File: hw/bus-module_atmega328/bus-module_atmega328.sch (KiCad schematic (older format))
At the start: 32 parts, among them J1 CONN_10X2, J2 CONN_7X2, J3 CONN-ISP-6, J5 CONN_1, J6 CONN_1, J7 CONN_1, J8 CONN_1, U1 ATMEGA328-TQFP32, U2 7,3728MHz, U3 25LC256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

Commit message: R2, R3, R4 100 Ohms
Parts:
- F1: symbol bus-module_atmega328-rescue:FUSE -> bus-module_atmega328-rescue:FUSE-bus-module_atmega328-rescue
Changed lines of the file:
@@
 B
 $Comp
-L bus-module_atmega328-rescue:FUSE F1
+L bus-module_atmega328-rescue:FUSE-bus-module_atmega328-rescue F1
 U 1 1 56648405
 P 8950 1200

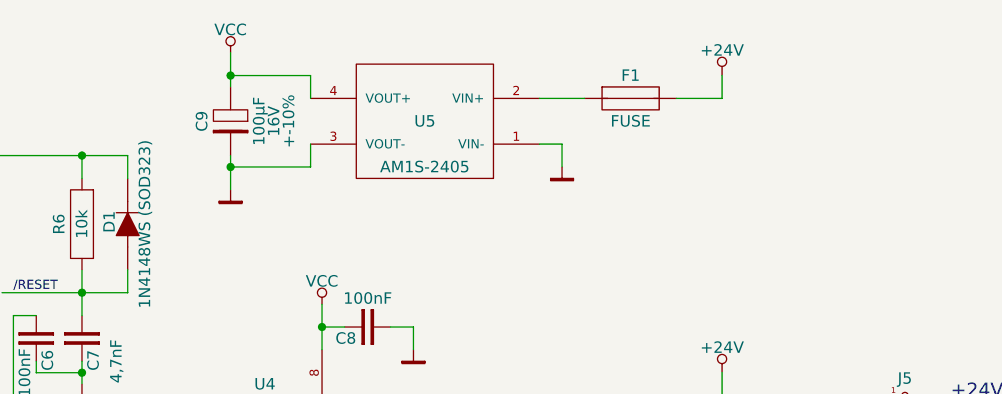
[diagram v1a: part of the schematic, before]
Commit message: Increase WAGO hole diameter, replace ELKO with keramic capacitor, Increase WAGO hole diameter, update footprints, update footprints, set Rev to C
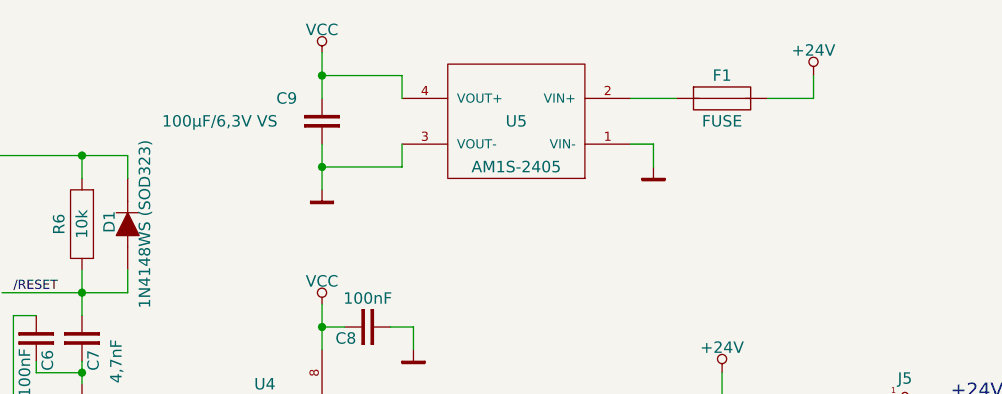
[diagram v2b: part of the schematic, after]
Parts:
- removed C9: 100µF, Capacitors:cp_smd_6.3, symbol standard:CP
- added C9: 100µF/6,3V VS, Capacitors_SMD:C_1206, symbol standard:C
- C1, C2, C3, C5, C6, C7, C8: footprint Housings_SOIC:SM0805 -> Capacitors_SMD:C_0805
- D1: footprint Diode:SOD323 -> Diode_SMD:D_SOD323
- D2: footprint Diode_SMD:SOT143 -> Diode_SMD:D_SOT143
- J5, J6, J7, J8: footprint Connector_Miscelleaneus:WAGO243 -> Connector_WAGO:WAGO243
- L1: footprint Housings_SOIC:SM0805 -> Inductor:L_0805
- R1, R2, R3, R4, R5, R6: footprint Housings_SOIC:SM0805 -> Resistor:R_0805
- U2: footprint Crystal:HC49-SMD -> Crystal:CRY_HC49_SMD
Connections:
- net GND: now also C9.2
- net VCC: now also C9.1
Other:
- moved on the sheet: F1, U5
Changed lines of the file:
@@
 Sheet 1 1
 Title "bus-module_atmega328"
-Date "2018-09-22"
-Rev "B"
+Date "2019-03-06"
+Rev "C"
 Comp "KoeWiBa"
 Comment1 ""
@@
 F 0 "J5" H 10150 2575 50  0000 C CNN
 F 1 "CONN_1" H 10150 2425 25  0000 C CNN
-F 2 "Connector_Miscelleaneus:WAGO243" H 10150 2500 60  0001 C CNN
+F 2 "Connector_WAGO:WAGO243" H 10150 2500 60  0001 C CNN
 F 3 "" H 10150 2500 60  0000 C CNN
 	1    10150 2500
@@
 F 0 "J6" H 10150 2775 50  0000 C CNN
 F 1 "CONN_1" H 10150 2625 25  0000 C CNN
-F 2 "Connector_Miscelleaneus:WAGO243" H 10150 2700 60  0001 C CNN
+F 2 "Connector_WAGO:WAGO243" H 10150 2700 60  0001 C CNN
 F 3 "" H 10150 2700 60  0000 C CNN
 	1    10150 2700
@@
 F 0 "J7" H 10150 2975 50  0000 C CNN
 F 1 "CONN_1" H 10150 2825 25  0000 C CNN
-F 2 "Connector_Miscelleaneus:WAGO243" H 10150 2900 60  0001 C CNN
+F 2 "Connector_WAGO:WAGO243" H 10150 2900 60  0001 C CNN
 F 3 "" H 10150 2900 60  0000 C CNN
 	1    10150 2900
@@
 F 0 "J8" H 10150 3175 50  0000 C CNN
 F 1 "CONN_1" H 10150 3025 25  0000 C CNN
-F 2 "Connector_Miscelleaneus:WAGO243" H 10150 3100 60  0001 C CNN
+F 2 "Connector_WAGO:WAGO243" H 10150 3100 60  0001 C CNN
 F 3 "" H 10150 3100 60  0000 C CNN
 	1    10150 3100
@@
 L ics_regulator:AM1S-2403 U5
 U 1 1 559D5CD1
-P 8050 1300
-F 0 "U5" H 8050 1300 50  0000 C CNN
-F 1 "AM1S-2405" H 8050 1100 50  0000 C CNN
-F 2 "DCDC_Converter:AM1S-XXXX_SIL4" H 8050 1500 25  0001 C CNN
-F 3 "" H 7300 1300 25  0001 C CNN
-	1    8050 1300
+P 8450 1300
+F 0 "U5" H 8450 1300 50  0000 C CNN
+F 1 "AM1S-2405" H 8450 1100 50  0000 C CNN
+F 2 "DCDC_Converter:AM1S-XXXX_SIL4" H 8450 1500 25  0001 C CNN
+F 3 "" H 7700 1300 25  0001 C CNN
+	1    8450 1300
 	-1   0    0    -1
-$EndComp
-$Comp
-L standard:CP C9
-U 1 1 559D5D78
-P 7200 1300
-F 0 "C9" H 7200 1175 50  0000 C CNN
-F 1 "100µF" H 7200 1425 50  0000 C CNN
-F 2 "Capacitors:cp_smd_6.3" H 7200 1300 60  0001 C CNN
-F 3 "" H 7200 1300 60  0000 C CNN
-F 4 "16V" H 7200 1490 50  0000 C CNN "Voltage"
-F 5 "+-10%" H 7200 1555 50  0000 C CNN "Tolrance"
-	1    7200 1300
-	0    1    1    0
 $EndComp
 $Comp
@@
 F 0 "C8" H 7850 2250 50  0000 L CNN
 F 1 "100nF" H 7800 2075 50  0000 C CNN
-F 2 "Housings_SOIC:SM0805" H 7800 2200 60  0001 C CNN
+F 2 "Capacitors_SMD:C_0805" H 7800 2200 60  0001 C CNN
 F 3 "" H 7800 2200 60  0000 C CNN
 	1    7800 2200
@@
 F 0 "C3" H 5000 1850 50  0000 L CNN
 F 1 "100nF" H 4800 1750 50  0000 C CNN
-F 2 "Housings_SOIC:SM0805" H 4950 1800 60  0001 C CNN
+F 2 "Capacitors_SMD:C_0805" H 4950 1800 60  0001 C CNN
 F 3 "" H 4950 1800 60  0000 C CNN
 	1    4950 1800
@@
 F 0 "C2" H 6500 4700 50  0000 L CNN
 F 1 "18pF" H 6550 4500 50  0000 C CNN
-F 2 "Housings_SOIC:SM0805" H 6450 4650 60  0001 C CNN
+F 2 "Capacitors_SMD:C_0805" H 6450 4650 60  0001 C CNN
 F 3 "" H 6450 4650 60  0000 C CNN
 	1    6450 4650
@@
 F 0 "C1" H 6500 4350 50  0000 L CNN
 F 1 "18pF" H 6550 4150 50  0000 C CNN
-F 2 "Housings_SOIC:SM0805" H 6450 4300 60  0001 C CNN
+F 2 "Capacitors_SMD:C_0805" H 6450 4300 60  0001 C CNN
 F 3 "" H 6450 4300 60  0000 C CNN
 	1    6450 4300
@@
 F 0 "C5" H 5250 6400 50  0000 L CNN
 F 1 "100nF" H 5200 6225 50  0000 C CNN
-F 2 "Housings_SOIC:SM0805" H 5200 6350 60  0001 C CNN
+F 2 "Capacitors_SMD:C_0805" H 5200 6350 60  0001 C CNN
 F 3 "" H 5200 6350 60  0000 C CNN
 	1    5200 6350
@@
 F 0 "U2" H 6475 4400 50  0000 C CNN
 F 1 "7,3728MHz" H 6500 4150 50  0000 C CNN
-F 2 "Crystal:HC49-SMD" H 6300 4300 60  0001 C CNN
+F 2 "Crystal:CRY_HC49_SMD" H 6300 4300 60  0001 C CNN
 F 3 "" H 6300 4300 60  0000 C CNN
 	1    6300 4300
@@
 F 0 "R4" H 4100 5700 50  0000 C CNN
 F 1 "100" H 4900 5700 50  0000 C CNN
-F 2 "Housings_SOIC:SM0805" H 4900 5700 60  0001 C CNN
+F 2 "Resistor:R_0805" H 4900 5700 60  0001 C CNN
 F 3 "" H 4900 5700 60  0000 C CNN
 	1    4900 5700
@@
 F 0 "R3" H 4100 5600 50  0000 C CNN
 F 1 "100" H 4900 5600 50  0000 C CNN
-F 2 "Housings_SOIC:SM0805" H 4900 5600 60  0001 C CNN
+F 2 "Resistor:R_0805" H 4900 5600 60  0001 C CNN
 F 3 "" H 4900 5600 60  0000 C CNN
 	1    4900 5600
@@
 F 0 "R2" H 4100 5500 50  0000 C CNN
 F 1 "100" H 4900 5500 50  0000 C CNN
-F 2 "Housings_SOIC:SM0805" H 4900 5500 60  0001 C CNN
+F 2 "Resistor:R_0805" H 4900 5500 60  0001 C CNN
 F 3 "" H 4900 5500 60  0000 C CNN
 	1    4900 5500
@@
 F 0 "R1" H 4550 6300 50  0000 C CNN
 F 1 "10k" H 4550 6400 50  0000 C CNN
-F 2 "Housings_SOIC:SM0805" H 4550 6400 60  0001 C CNN
+F 2 "Resistor:R_0805" H 4550 6400 60  0001 C CNN
 F 3 "" H 4550 6400 60  0000 C CNN
 	1    4550 6400
@@
 F 0 "R5" H 5900 6300 50  0000 C CNN
 F 1 "10k" H 5900 6400 50  0000 C CNN
-F 2 "Housings_SOIC:SM0805" H 5900 6400 60  0001 C CNN
+F 2 "Resistor:R_0805" H 5900 6400 60  0001 C CNN
 F 3 "" H 5900 6400 60  0000 C CNN
 	1    5900 6400
@@
 F 0 "C6" H 6400 2300 50  0000 L CNN
 F 1 "100nF" H 6500 2200 50  0000 C CNN
-F 2 "Housings_SOIC:SM0805" H 6350 2250 60  0001 C CNN
+F 2 "Capacitors_SMD:C_0805" H 6350 2250 60  0001 C CNN
 F 3 "" H 6350 2250 60  0000 C CNN
 	1    6350 2250
@@
 F 0 "C7" H 6600 2300 50  0000 L CNN
 F 1 "4,7nF" H 6650 2400 50  0000 C CNN
-F 2 "Housings_SOIC:SM0805" H 6550 2250 60  0001 C CNN
+F 2 "Capacitors_SMD:C_0805" H 6550 2250 60  0001 C CNN
 F 3 "" H 6550 2250 60  0000 C CNN
 	1    6550 2250
@@
 F 0 "R6" H 6550 1650 50  0000 C CNN
 F 1 "10k" H 6550 1750 50  0000 C CNN
-F 2 "Housings_SOIC:SM0805" H 6550 1750 60  0001 C CNN
+F 2 "Resistor:R_0805" H 6550 1750 60  0001 C CNN
 F 3 "" H 6550 1750 60  0000 C CNN
 	1    6550 1750
@@
 F 0 "L1" H 5400 1700 50  0000 L CNN
 F 1 "10µH" H 5400 1885 50  0000 L CNN
-F 2 "Housings_SOIC:SM0805" H 5500 1800 60  0001 C CNN
+F 2 "Inductor:L_0805" H 5500 1800 60  0001 C CNN
 F 3 "" H 5500 1800 60  0000 C CNN
 	1    5500 1800
@@
 	6550 1450 6550 1550
 Wire Wire Line
-	7550 1200 7550 1100
-Wire Wire Line
-	7550 1100 7200 1100
-Wire Wire Line
-	7200 1000 7200 1100
-Wire Wire Line
-	7550 1400 7550 1500
-Wire Wire Line
-	7550 1500 7200 1500
-Wire Wire Line
-	7200 1450 7200 1500
+	7950 1200 7950 1100
+Wire Wire Line
+	7950 1100 7600 1100
+Wire Wire Line
+	7600 1000 7600 1100
+Wire Wire Line
+	7950 1400 7950 1500
+Wire Wire Line
+	7950 1500 7600 1500
 $Comp
 L power:+24V #PWR010
 U 1 1 55A0FF09
-P 9350 1100
-F 0 "#PWR010" H 9350 1300 50  0001 C CNN
-F 1 "+24V" H 9350 1210 50  0000 C CNN
-F 2 "" H 9350 1100 60  0000 C CNN
-F 3 "" H 9350 1100 60  0000 C CNN
-	1    9350 1100
+P 9750 1100
+F 0 "#PWR010" H 9750 1300 50  0001 C CNN
+F 1 "+24V" H 9750 1210 50  0000 C CNN
+F 2 "" H 9750 1100 60  0000 C CNN
+F 3 "" H 9750 1100 60  0000 C CNN
+	1    9750 1100
 	1    0    0    -1
 $EndComp
@@
 L power:GND #PWR011
 U 1 1 55A10203
-P 8650 1500
-F 0 "#PWR011" H 8650 1300 50  0001 C CNN
-F 1 "GND" H 8650 1390 50  0001 C CNN
-F 2 "" H 8650 1500 60  0000 C CNN
-F 3 "" H 8650 1500 60  0000 C CNN
-	1    8650 1500
+P 9050 1500
+F 0 "#PWR011" H 9050 1300 50  0001 C CNN
+F 1 "GND" H 9050 1390 50  0001 C CNN
+F 2 "" H 9050 1500 60  0000 C CNN
+F 3 "" H 9050 1500 60  0000 C CNN
+	1    9050 1500
 	1    0    0    -1
 $EndComp
@@
 L power:GND #PWR012
 U 1 1 55A10383
-P 7200 1600
-F 0 "#PWR012" H 7200 1400 50  0001 C CNN
-F 1 "GND" H 7200 1490 50  0001 C CNN
-F 2 "" H 7200 1600 60  0000 C CNN
-F 3 "" H 7200 1600 60  0000 C CNN
-	1    7200 1600
+P 7600 1600
+F 0 "#PWR012" H 7600 1400 50  0001 C CNN
+F 1 "GND" H 7600 1490 50  0001 C CNN
+F 2 "" H 7600 1600 60  0000 C CNN
+F 3 "" H 7600 1600 60  0000 C CNN
+	1    7600 1600
 	1    0    0    -1
 $EndComp
@@
 	9950 4100 9950 3100
 Wire Wire Line
-	9350 1100 9350 1200
-Wire Wire Line
-	8550 1400 8650 1400
-Wire Wire Line
-	8650 1400 8650 1500
-Connection ~ 7200 1500
-Connection ~ 7200 1100
+	9750 1100 9750 1200
+Wire Wire Line
+	8950 1400 9050 1400
+Wire Wire Line
+	9050 1400 9050 1500
 Text Notes 10350 3100 0    60   ~ 0
 +24V\n\nA\n\nB \n\nGND
@@
 F 0 "D1" H 6760 1830 50  0000 C CNN
 F 1 "1N4148WS (SOD323)" H 6750 1675 50  0000 C CNN
-F 2 "Diode:SOD323" H 6750 1750 60  0001 C CNN
+F 2 "Diode_SMD:D_SOD323" H 6750 1750 60  0001 C CNN
 F 3 "" H 6750 1750 60  0000 C CNN
 	1    6750 1750
@@
 F 0 "D2" H 9125 3450 50  0000 C CNN
 F 1 "SEMTECH SR05" H 9050 4050 50  0000 C CNN
-F 2 "Diode_SMD:SOT143" H 9050 3700 60  0001 C CNN
+F 2 "Diode_SMD:D_SOT143" H 9050 3700 60  0001 C CNN
 F 3 "" H 9050 3700 60  0000 C CNN
 	1    9050 3700
@@
 L power:VCC #PWR018
 U 1 1 5605057B
-P 7200 1000
-F 0 "#PWR018" H 7200 1175 50  0001 C CNN
-F 1 "VCC" H 7200 1100 50  0000 C CNN
-F 2 "" H 7200 1000 60  0000 C CNN
-F 3 "" H 7200 1000 60  0000 C CNN
-	1    7200 1000
+P 7600 1000
+F 0 "#PWR018" H 7600 1175 50  0001 C CNN
+F 1 "VCC" H 7600 1100 50  0000 C CNN
+F 2 "" H 7600 1000 60  0000 C CNN
+F 3 "" H 7600 1000 60  0000 C CNN
+	1    7600 1000
 	1    0    0    -1
 $EndComp
@@
 L bus-module_atmega328-rescue:FUSE-bus-module_atmega328-rescue F1
 U 1 1 56648405
-P 8950 1200
-F 0 "F1" H 8950 1300 50  0000 C CNN
-F 1 "FUSE" H 8950 1100 50  0000 C CNN
-F 2 "Resistor:R_1812" H 8950 1200 60  0001 C CNN
-F 3 "" H 8950 1200 60  0000 C CNN
-	1    8950 1200
+P 9350 1200
+F 0 "F1" H 9350 1300 50  0000 C CNN
+F 1 "FUSE" H 9350 1100 50  0000 C CNN
+F 2 "Resistor:R_1812" H 9350 1200 60  0001 C CNN
+F 3 "" H 9350 1200 60  0000 C CNN
+	1    9350 1200
 	1    0    0    -1
 $EndComp
@@
 $EndComp
 Wire Wire Line
-	8750 1200 8550 1200
-Wire Wire Line
-	9350 1200 9150 1200
+	9150 1200 8950 1200
+Wire Wire Line
+	9750 1200 9550 1200
 Wire Wire Line
 	7600 2200 7600 2300
@@
 	6550 2400 6550 2450
 Wire Wire Line
-	7200 1500 7200 1600
-Wire Wire Line
-	7200 1100 7200 1150
+	7600 1500 7600 1600
 Wire Wire Line
 	5350 4850 5250 4850
@@
 Wire Wire Line
 	6550 1450 6750 1450
+$Comp
+L standard:C C9
+U 1 1 5C813758
+P 7600 1300
+F 0 "C9" V 7500 1100 50  0000 L CNN
+F 1 "100µF/6,3V VS" V 7600 600 50  0000 L CNN
+F 2 "Capacitors_SMD:C_1206" H 7600 1300 60  0001 C CNN
+F 3 "" H 7600 1300 60  0000 C CNN
+	1    7600 1300
+	0    1    1    0
+$EndComp
+Wire Wire Line
+	7600 1200 7600 1100
+Connection ~ 7600 1100
+Wire Wire Line
+	7600 1400 7600 1500
+Connection ~ 7600 1500
 Wire Bus Line
 	5400 5600 5400 5800
